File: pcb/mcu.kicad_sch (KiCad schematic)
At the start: 4 parts, among them J1 Conn_01x04, SW1 TS-1088-AR02016, U3 STC8H1K08-QFN20

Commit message: Redo some of the layout, move button
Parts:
- added TP3, TP4: TestPoint, TestPoint:TestPoint_Pad_D1.0mm, symbol Connector:TestPoint
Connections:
- net UART_RX: now also TP4.1
- net UART_TX: now also TP3.1
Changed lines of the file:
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@@
+		)
+	)
+	(label "UART_RX"
+		(at 55.88 62.23 0)
+		(effects
+			(font
+				(size 1.27 1.27)
+			)
+			(justify left bottom)
 		)
 	)
@@
 	(label "pwm8"
 		(at 195.58 35.56 0)
+		(effects
+			(font
+				(size 1.27 1.27)
+			)
+			(justify left bottom)
+		)
+	)
+	(label "UART_TX"
+		(at 55.88 55.88 0)
 		(effects
 			(font
@@
 	)
 	(symbol
+		(lib_id "Connector:TestPoint")
+		(at 55.88 55.88 90)
+		(unit 1)
+		(body_style 1)
+		(exclude_from_sim no)
+		(in_bom yes)
+		(on_board yes)
+		(in_pos_files yes)
+		(dnp no)
+		(fields_autoplaced yes)
+		(property "Reference" "TP3"
+			(at 52.578 51.1005 90)
+			(show_name no)
+			(do_not_autoplace no)
+			(effects
+				(font
+					(size 1.27 1.27)
+				)
+			)
+		)
+		(property "Value" "TestPoint"
+			(at 52.578 53.5248 90)
+			(show_name no)
+			(do_not_autoplace no)
+			(effects
+				(font
+					(size 1.27 1.27)
+				)
+			)
+		)
+		(property "Footprint" "TestPoint:TestPoint_Pad_D1.0mm"
+			(at 55.88 50.8 0)
+			(hide yes)
+			(show_name no)
+			(do_not_autoplace no)
+			(effects
+				(font
+					(size 1.27 1.27)
+				)
+			)
+		)
+		(property "Datasheet" ""
+			(at 55.88 50.8 0)
+			(hide yes)
+			(show_name no)
+			(do_not_autoplace no)
+			(effects
+				(font
+					(size 1.27 1.27)
+				)
+			)
+		)
+		(property "Description" "test point"
+			(at 55.88 55.88 0)
+			(hide yes)
+			(show_name no)
+			(do_not_autoplace no)
+			(effects
+				(font
+					(size 1.27 1.27)
+				)
+			)
+		)
+		(pin "1"
+		)
+		(instances
+			(project "nametag"
+				(path "/a7c50b29-e914-4aee-9ec8-81f37f7bd068/858a59c4-d6e3-4a1e-955d-510d1161f2bb"
+					(reference "TP3")
+					(unit 1)
+				)
+			)
+		)
+	)
+	(symbol
 		(lib_id "stc8h:STC8H1K08-QFN20")
 		(at 140.97 38.1 0)
@@
 					(unit 1)
 				)
+			)
+		)
+	)
+	(symbol
+		(lib_id "Connector:TestPoint")
+		(at 55.88 62.23 90)
+		(unit 1)
+		(body_style 1)
+		(exclude_from_sim no)
+		(in_bom yes)
+		(on_board yes)
+		(in_pos_files yes)
+		(dnp no)
+		(fields_autoplaced yes)
+		(property "Reference" "TP4"
+			(at 52.578 57.4505 90)
+			(show_name no)
+			(do_not_autoplace no)
+			(effects
+				(font
+					(size 1.27 1.27)
+				)
+			)
+		)
+		(property "Value" "TestPoint"
+			(at 52.578 59.8748 90)
+			(show_name no)
+			(do_not_autoplace no)
+			(effects
+				(font
+					(size 1.27 1.27)
+				)
+			)
+		)
+		(property "Footprint" "TestPoint:TestPoint_Pad_D1.0mm"
+			(at 55.88 57.15 0)
+			(hide yes)
+			(show_name no)
+			(do_not_autoplace no)
+			(effects
+				(font
+					(size 1.27 1.27)
+				)
+			)
+		)
+		(property "Datasheet" ""
+			(at 55.88 57.15 0)
+			(hide yes)
+			(show_name no)
+			(do_not_autoplace no)
+			(effects
+				(font
+					(size 1.27 1.27)
+				)
+			)
+		)
+		(property "Description" "test point"
+			(at 55.88 62.23 0)
+			(hide yes)
+			(show_name no)
+			(do_not_autoplace no)
+			(effects
+				(font
+					(size 1.27 1.27)
+				)
+			)
+		)
+		(pin "1"
+		)
+		(instances
+			(project "nametag"
+				(path "/a7c50b29-e914-4aee-9ec8-81f37f7bd068/858a59c4-d6e3-4a1e-955d-510d1161f2bb"
+					(reference "TP4")
+					(unit 1)
+				)

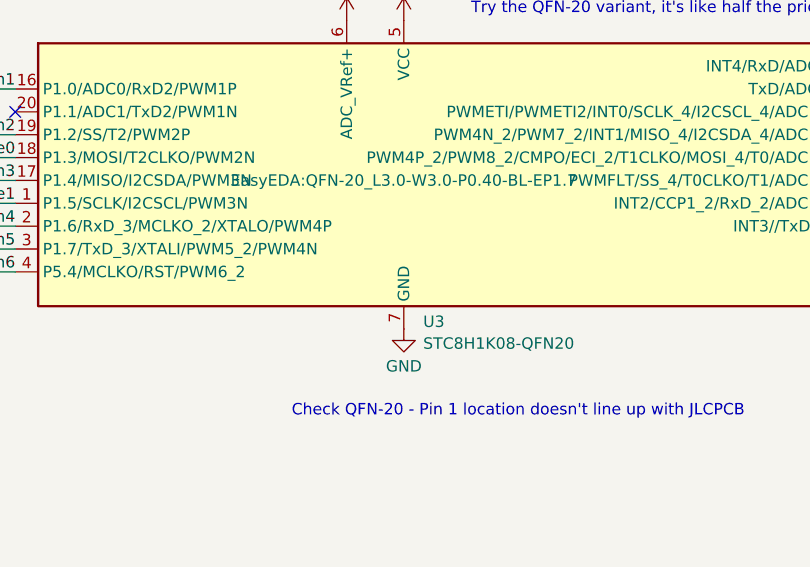
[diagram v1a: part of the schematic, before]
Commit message: Submit files to JLCPCB for manufacture
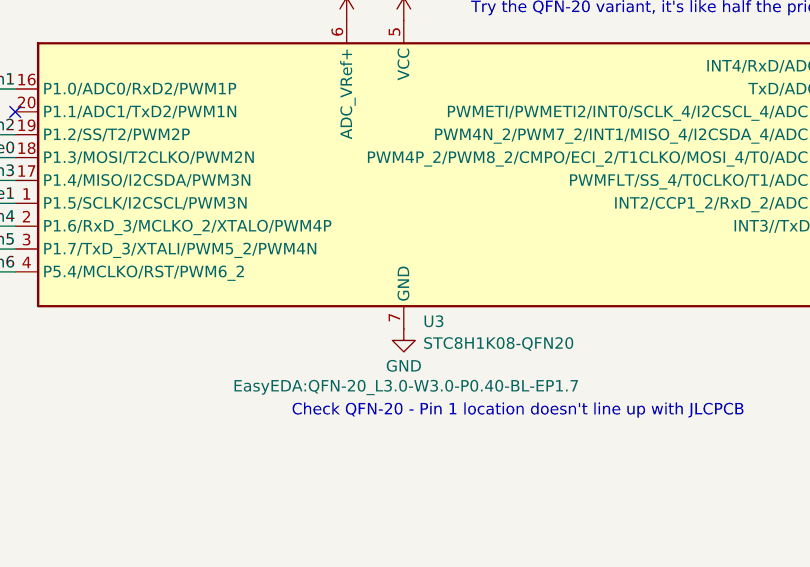
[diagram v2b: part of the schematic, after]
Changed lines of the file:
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@@
 		(in_pos_files yes)
 		(dnp no)
-		(fields_autoplaced yes)
 		(property "Reference" "U3"
 			(at 143.1133 53.7901 0)
@@
 		)
 		(property "Footprint" "EasyEDA:QFN-20_L3.0-W3.0-P0.40-BL-EP1.7"
-			(at 140.97 38.1 0)
+			(at 141.224 60.96 0)
 			(show_name no)
 			(do_not_autoplace no)
